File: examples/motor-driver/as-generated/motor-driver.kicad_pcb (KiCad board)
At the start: 2 copper layers, 88 x 50 mm, 19 parts, among them J1 VM 2.7-10.8V, J2 MOTOR A, J3 MOTOR B, J4 LOGIC, U1 DRV8833PW

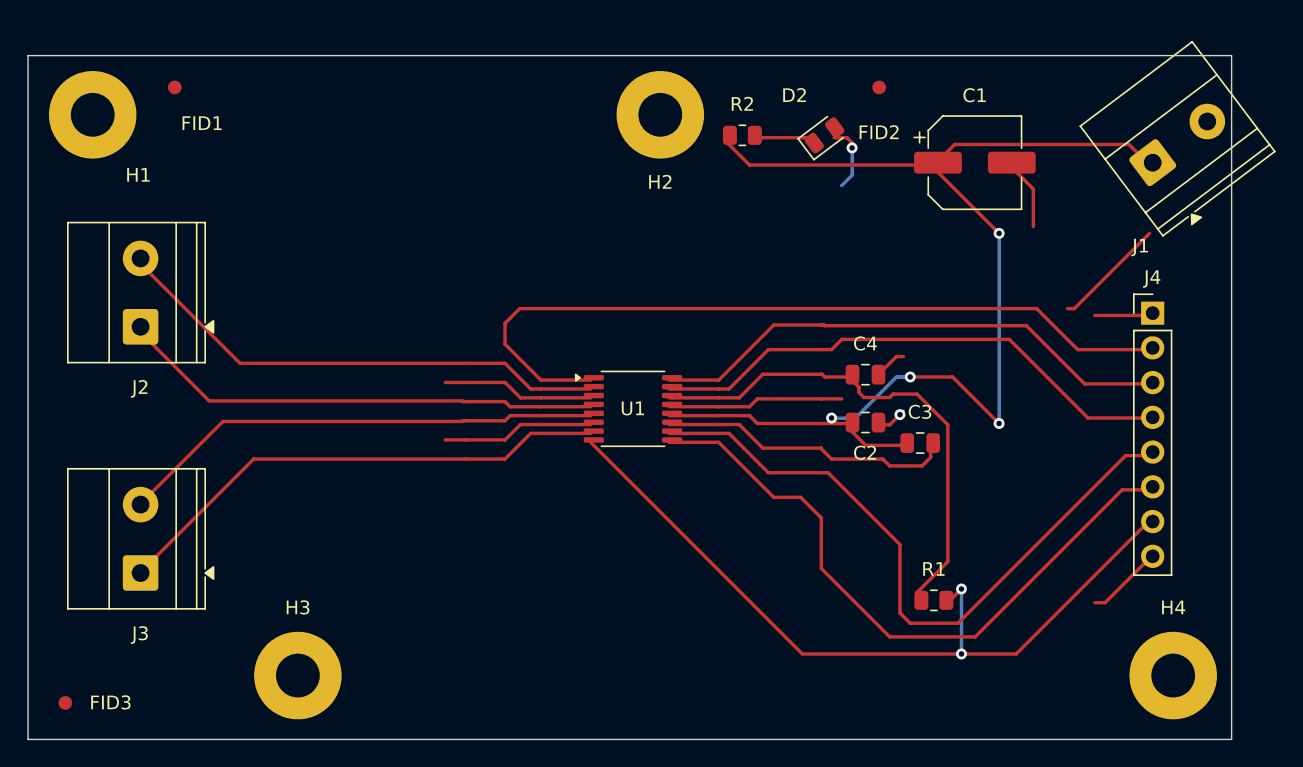
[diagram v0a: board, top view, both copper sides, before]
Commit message: Rebuild golden layouts and gate floorplan quality
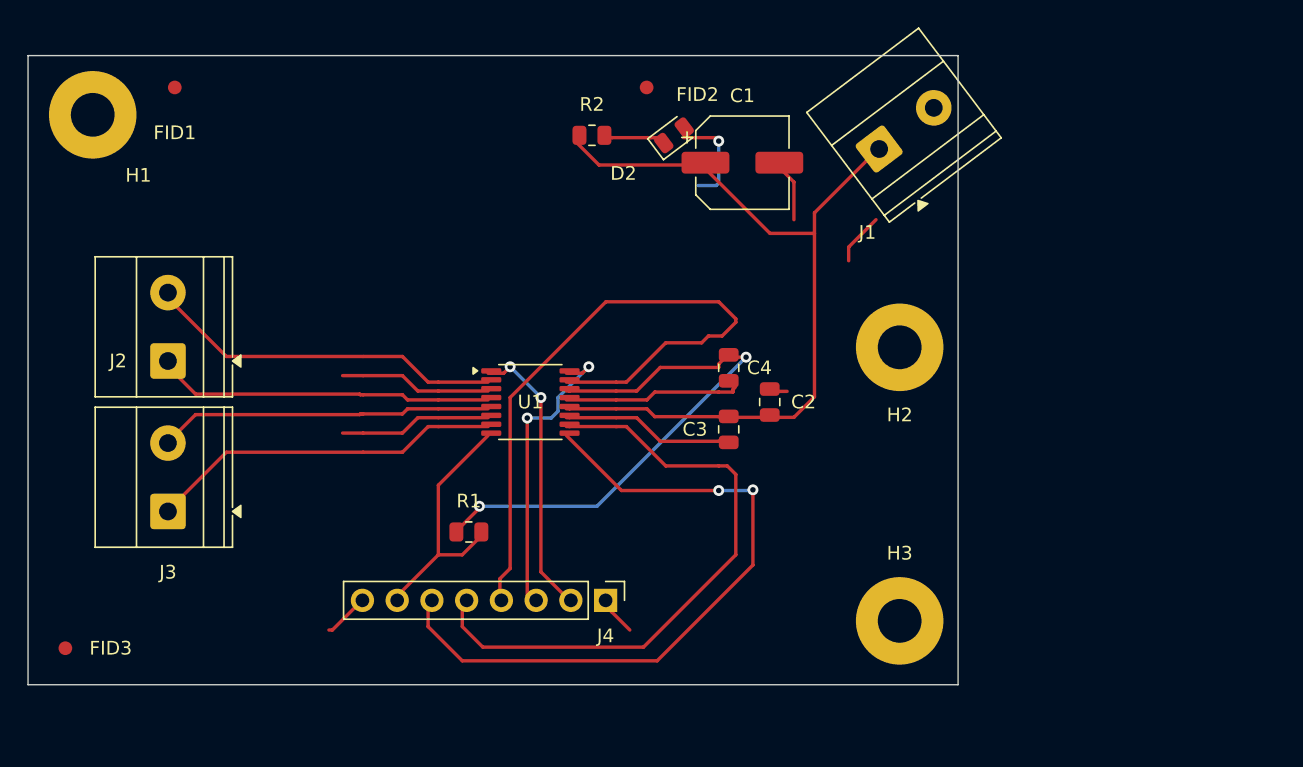
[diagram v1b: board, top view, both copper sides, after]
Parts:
- removed H4: M3, MountingHole:MountingHole_3.2mm_M3_Pad
- moved J4 45.2 mm to (142.2, 99.8), turned to 270 degrees
- moved H3 44.2 mm to (163.7, 101.3)
- moved R1 34.4 mm to (132.2, 94.8)
- moved H2 24.4 mm to (163.7, 81.3)
- moved J1 20.0 mm to (162.2, 66.8)
- moved C1 17.0 mm to (152.2, 67.8)
- moved FID2 17.0 mm to (145.2, 62.3), turned to 37 degrees
- moved C3 14.0 mm to (151.2, 87.3), turned to 270 degrees
- moved D2 11.0 mm to (147.2, 65.8)
- moved R2 11.0 mm to (141.2, 65.8)
- moved C4 10.0 mm to (151.2, 82.8), turned to 270 degrees
- moved U1 7.52 mm to (136.7, 85.3)
- moved C2 7.16 mm to (154.2, 85.3), turned to 90 degrees
- moved J3 4.92 mm to (110.2, 93.3)
- moved FID3 4.00 mm to (102.7, 103.3)
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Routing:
- net /nFAULT: track 57.7 -> 18.9 mm, vias 2 -> 0
- net /nSLEEP: track 57.7 -> 20.8 mm, vias 0 -> 2
- net /VM: track 87.9 -> 59.5 mm, vias 4 -> 0
- net /AIN1: track 38.6 -> 22.9 mm, vias 0 -> 2
- net /BOUT1: track 37.4 -> 26.3 mm
- net /BOUT2: track 35.9 -> 24.7 mm
- net /AOUT1: track 37.0 -> 26.3 mm
- net /AOUT2: track 35.5 -> 24.7 mm
- net /AIN2: track 39.1 -> 49.7 mm
- net /VCP: track 21.6 -> 12.5 mm
- net /LED_A: track 9.05 -> 4.15 mm, vias 1 -> 0
- net /VINT: track 37.1 -> 41.2 mm, vias 0 -> 2
- net GND: track 63.1 -> 59.1 mm
- net /BIN2: track 48.9 -> 44.9 mm
- net /BIN1: track 47.7 -> 50.3 mm, vias 0 -> 2
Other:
- board size 88 x 50 mm -> 68 x 46 mm

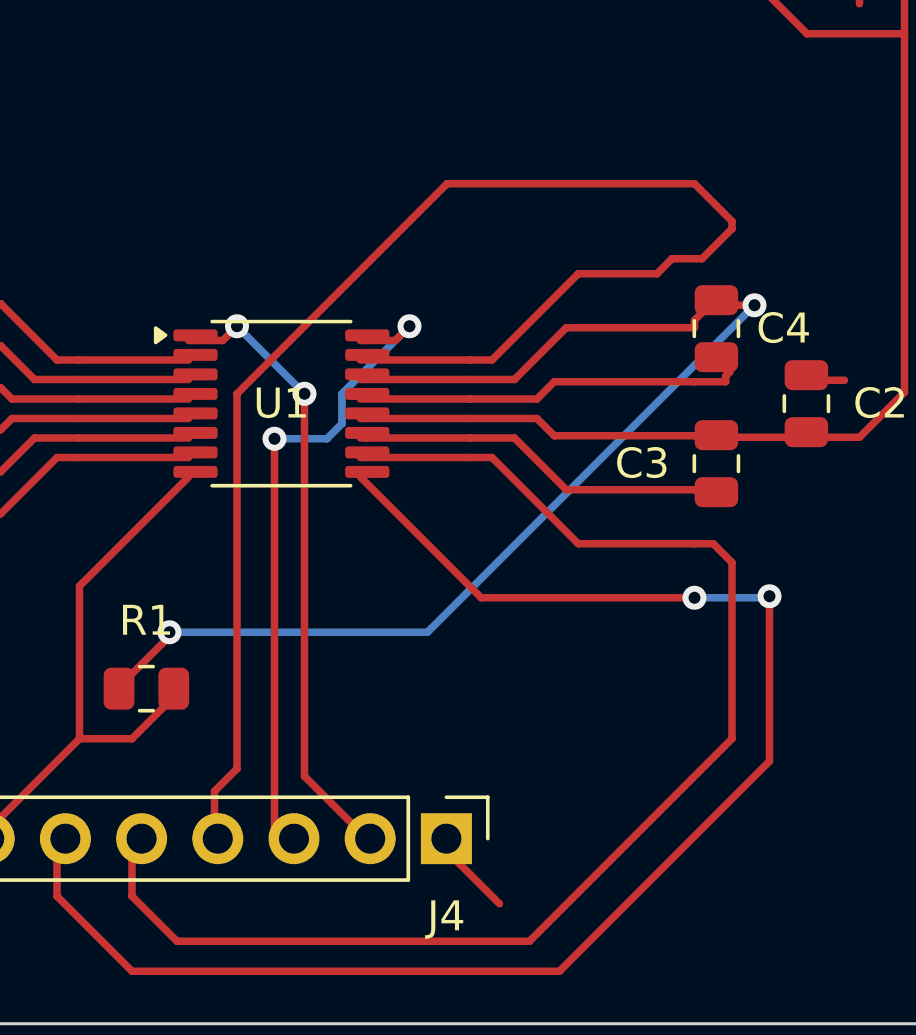
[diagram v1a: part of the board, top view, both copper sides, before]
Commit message: Use canonical fills and close motor return path
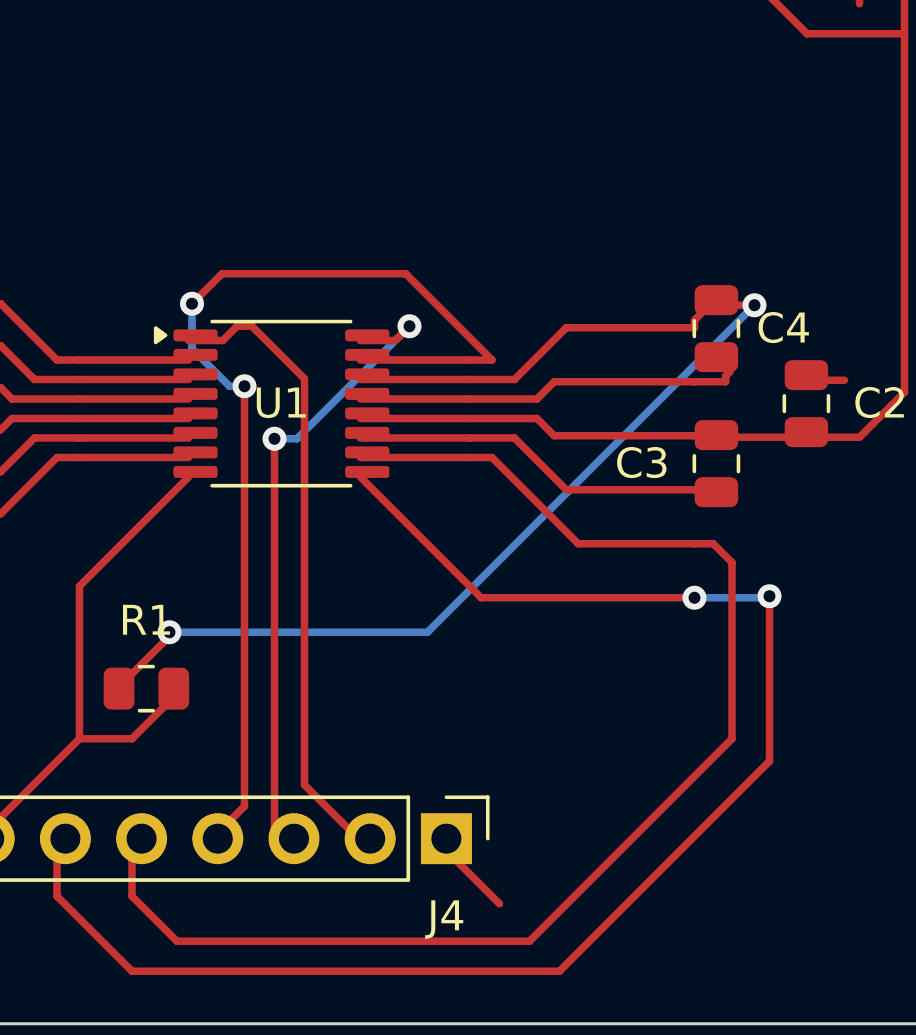
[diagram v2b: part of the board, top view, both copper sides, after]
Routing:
- net /AIN2: track 49.7 -> 35.5 mm, vias 0 -> 2
- net /AIN1: track 22.9 -> 21.6 mm
- net /nSLEEP: track 20.8 -> 21.1 mm, vias 2 -> 0
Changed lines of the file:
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@@
 	(segment (start 150.5 69.32) (end 150.32 69.5) (width 0.25) (layer "B.Cu") (net 1))
 	(segment (start 150.32 69.5) (end 149.0 69.5) (width 0.25) (layer "B.Cu") (net 1))
-	(segment (start 133.6375 83.225) (end 133.8675 83.225) (width 0.25) (layer "F.Cu") (net 15))
-	(segment (start 133.8675 83.225) (end 134.775 83.225) (width 0.25) (layer "F.Cu") (net 15))
-	(segment (start 134.775 83.225) (end 135.25 82.75) (width 0.25) (layer "F.Cu") (net 15))
 	(segment (start 133.6375 83.875) (end 130.0 83.875) (width 0.25) (layer "F.Cu") (net 4))
 	(segment (start 130.0 83.875) (end 129.25 83.875) (width 0.25) (layer "F.Cu") (net 4))
@@
 	(segment (start 133.6375 87.775) (end 130.0 91.4125) (width 0.25) (layer "F.Cu") (net 14))
 	(segment (start 130.0 91.4125) (end 130.0 96.5) (width 0.25) (layer "F.Cu") (net 14))
-	(segment (start 139.3625 83.225) (end 139.5925 83.225) (width 0.25) (layer "F.Cu") (net 2))
-	(segment (start 139.5925 83.225) (end 140.525 83.225) (width 0.25) (layer "F.Cu") (net 2))
-	(segment (start 140.525 83.225) (end 141.0 82.75) (width 0.25) (layer "F.Cu") (net 2))
 	(segment (start 139.3625 83.875) (end 139.5925 83.875) (width 0.25) (layer "F.Cu") (net 3))
 	(segment (start 139.5925 83.875) (end 143.0 83.875) (width 0.25) (layer "F.Cu") (net 3))
 	(segment (start 143.0 83.875) (end 143.75 83.875) (width 0.25) (layer "F.Cu") (net 3))
-	(segment (start 143.75 83.875) (end 146.625 81.0) (width 0.25) (layer "F.Cu") (net 3))
-	(segment (start 146.625 81.0) (end 149.25 81.0) (width 0.25) (layer "F.Cu") (net 3))
-	(segment (start 149.25 81.0) (end 149.75 80.5) (width 0.25) (layer "F.Cu") (net 3))
-	(segment (start 149.75 80.5) (end 150.75 80.5) (width 0.25) (layer "F.Cu") (net 3))
-	(segment (start 150.75 80.5) (end 151.75 79.5) (width 0.25) (layer "F.Cu") (net 3))
-	(segment (start 151.75 79.5) (end 151.75 79.25) (width 0.25) (layer "F.Cu") (net 3))
-	(segment (start 151.75 79.25) (end 150.5 78.0) (width 0.25) (layer "F.Cu") (net 3))
-	(segment (start 150.5 78.0) (end 142.25 78.0) (width 0.25) (layer "F.Cu") (net 3))
-	(segment (start 142.25 78.0) (end 135.25 85.0) (width 0.25) (layer "F.Cu") (net 3))
-	(segment (start 135.25 85.0) (end 135.25 97.5) (width 0.25) (layer "F.Cu") (net 3))
-	(segment (start 135.25 97.5) (end 134.5 98.25) (width 0.25) (layer "F.Cu") (net 3))
-	(segment (start 134.5 98.25) (end 134.5 99.75) (width 0.25) (layer "F.Cu") (net 3))
-	(segment (start 134.5 99.75) (end 134.5 99.83) (width 0.25) (layer "F.Cu") (net 3))
-	(segment (start 134.5 99.83) (end 134.5 99.88) (width 0.25) (layer "F.Cu") (net 3))
-	(segment (start 134.5 99.88) (end 134.38 100.0) (width 0.25) (layer "F.Cu") (net 3))
+	(segment (start 143.75 83.875) (end 140.875 81.0) (width 0.25) (layer "F.Cu") (net 3))
+	(segment (start 140.875 81.0) (end 134.75 81.0) (width 0.25) (layer "F.Cu") (net 3))
+	(segment (start 134.75 81.0) (end 133.75 82.0) (width 0.25) (layer "F.Cu") (net 3))
 	(segment (start 139.3625 84.525) (end 139.5925 84.525) (width 0.25) (layer "F.Cu") (net 12))
 	(segment (start 139.5925 84.525) (end 143.0 84.525) (width 0.25) (layer "F.Cu") (net 12))
@@
 	(segment (start 139.3625 87.775) (end 143.3875 91.8) (width 0.25) (layer "F.Cu") (net 6))
 	(segment (start 143.3875 91.8) (end 150.5 91.8) (width 0.25) (layer "F.Cu") (net 6))
+	(segment (start 139.3625 83.225) (end 139.5925 83.225) (width 0.25) (layer "F.Cu") (net 2))
+	(segment (start 139.5925 83.225) (end 140.525 83.225) (width 0.25) (layer "F.Cu") (net 2))
+	(segment (start 140.525 83.225) (end 141.0 82.75) (width 0.25) (layer "F.Cu") (net 2))
 	(segment (start 157.5 73.0) (end 157.5 71.5) (width 0.25) (layer "F.Cu") (net 13))
 	(segment (start 157.5 71.5) (end 161.2929 67.7071) (width 0.25) (layer "F.Cu") (net 13))
@@
 	(segment (start 145.5292 66.0) (end 145.7958 66.0) (width 0.25) (layer "F.Cu") (net 10))
 	(segment (start 145.7958 66.0) (end 146.0625 66.0) (width 0.25) (layer "F.Cu") (net 10))
-	(segment (start 141.0 82.75) (end 138.75 85.0) (width 0.25) (layer "B.Cu") (net 2))
-	(segment (start 138.75 85.0) (end 138.75 86.0) (width 0.25) (layer "B.Cu") (net 2))
-	(segment (start 138.75 86.0) (end 138.25 86.5) (width 0.25) (layer "B.Cu") (net 2))
-	(segment (start 138.25 86.5) (end 136.5 86.5) (width 0.25) (layer "B.Cu") (net 2))
-	(segment (start 136.5 86.5) (end 136.5 99.83) (width 0.25) (layer "F.Cu") (net 2))
-	(segment (start 136.5 99.83) (end 136.5 100.0) (width 0.25) (layer "F.Cu") (net 2))
-	(segment (start 136.5 100.0) (end 136.75 100.25) (width 0.25) (layer "F.Cu") (net 2))
-	(segment (start 136.75 100.25) (end 137.0 100.25) (width 0.25) (layer "F.Cu") (net 2))
-	(segment (start 137.0 100.25) (end 137.0 100.08) (width 0.25) (layer "F.Cu") (net 2))
-	(segment (start 137.0 100.08) (end 136.95 100.03) (width 0.25) (layer "F.Cu") (net 2))
-	(segment (start 136.95 100.03) (end 136.92 100.0) (width 0.25) (layer "F.Cu") (net 2))
+	(segment (start 141.0 82.75) (end 137.25 86.5) (width 0.25) (layer "B.Cu") (net 2))
+	(segment (start 137.25 86.5) (end 136.5 86.5) (width 0.25) (layer "B.Cu") (net 2))
+	(segment (start 136.5 86.5) (end 136.5 99.58) (width 0.25) (layer "F.Cu") (net 2))
+	(segment (start 136.5 99.58) (end 136.668 99.748) (width 0.25) (layer "F.Cu") (net 2))
+	(segment (start 136.668 99.748) (end 136.752 99.832) (width 0.25) (layer "F.Cu") (net 2))
+	(segment (start 136.752 99.832) (end 136.836 99.916) (width 0.25) (layer "F.Cu") (net 2))
+	(segment (start 136.836 99.916) (end 136.92 100.0) (width 0.25) (layer "F.Cu") (net 2))
+	(segment (start 133.75 82.0) (end 133.75 83.5) (width 0.25) (layer "B.Cu") (net 3))
+	(segment (start 133.75 83.5) (end 135.0 84.75) (width 0.25) (layer "B.Cu") (net 3))
+	(segment (start 135.0 84.75) (end 135.5 84.75) (width 0.25) (layer "B.Cu") (net 3))
+	(segment (start 135.5 84.75) (end 135.5 98.75) (width 0.25) (layer "F.Cu") (net 3))
+	(segment (start 135.5 98.75) (end 134.5 99.75) (width 0.25) (layer "F.Cu") (net 3))
+	(segment (start 134.5 99.75) (end 134.5 99.83) (width 0.25) (layer "F.Cu") (net 3))
+	(segment (start 134.5 99.83) (end 134.5 99.88) (width 0.25) (layer "F.Cu") (net 3))
+	(segment (start 134.5 99.88) (end 134.38 100.0) (width 0.25) (layer "F.Cu") (net 3))
 	(segment (start 150.5 91.8) (end 152.95 91.8) (width 0.25) (layer "B.Cu") (net 6))
 	(segment (start 152.95 91.8) (end 153.0 91.75) (width 0.25) (layer "B.Cu") (net 6))
@@
 	(segment (start 129.25 100.25) (end 129.25 100.05) (width 0.25) (layer "F.Cu") (net 6))
 	(segment (start 129.25 100.05) (end 129.3 100.0) (width 0.25) (layer "F.Cu") (net 6))
-	(segment (start 135.25 82.75) (end 137.5 85.0) (width 0.25) (layer "B.Cu") (net 15))
-	(segment (start 137.5 85.0) (end 137.5 97.75) (width 0.25) (layer "F.Cu") (net 15))
-	(segment (start 137.5 97.75) (end 139.5 99.75) (width 0.25) (layer "F.Cu") (net 15))
-	(segment (start 139.5 99.75) (end 139.5 99.83) (width 0.25) (layer "F.Cu") (net 15))
-	(segment (start 139.5 99.83) (end 139.5 99.96) (width 0.25) (layer "F.Cu") (net 15))
-	(segment (start 139.5 99.96) (end 139.46 100.0) (width 0.25) (layer "F.Cu") (net 15))
+	(segment (start 133.6375 83.225) (end 133.8675 83.225) (width 0.25) (layer "F.Cu") (net 15))
+	(segment (start 133.8675 83.225) (end 134.775 83.225) (width 0.25) (layer "F.Cu") (net 15))
+	(segment (start 134.775 83.225) (end 135.25 82.75) (width 0.25) (layer "F.Cu") (net 15))
+	(segment (start 135.25 82.75) (end 135.75 82.75) (width 0.25) (layer "F.Cu") (net 15))
+	(segment (start 135.75 82.75) (end 137.5 84.5) (width 0.25) (layer "F.Cu") (net 15))
+	(segment (start 137.5 84.5) (end 137.5 98.04) (width 0.25) (layer "F.Cu") (net 15))
+	(segment (start 137.5 98.04) (end 138.7529 99.2929) (width 0.25) (layer "F.Cu") (net 15))
+	(segment (start 138.7529 99.2929) (end 138.9886 99.5286) (width 0.25) (layer "F.Cu") (net 15))
+	(segment (start 138.9886 99.5286) (end 139.2243 99.7643) (width 0.25) (layer "F.Cu") (net 15))
+	(segment (start 139.2243 99.7643) (end 139.46 100.0) (width 0.25) (layer "F.Cu") (net 15))
 	(segment (start 132.9125 95.0) (end 132.9125 95.1625) (width 0.25) (layer "F.Cu") (net 14))
 	(segment (start 132.9125 95.1625) (end 133.0 95.25) (width 0.25) (layer "F.Cu") (net 14))
@@
 	(via (at 136.5 86.5) (size 0.8) (drill 0.4) (layers "F.Cu" "B.Cu") (net 2))
 	(via (at 141.0 82.75) (size 0.8) (drill 0.4) (layers "F.Cu" "B.Cu") (net 2))
+	(via (at 133.75 82.0) (size 0.8) (drill 0.4) (layers "F.Cu" "B.Cu") (net 3))
+	(via (at 135.5 84.75) (size 0.8) (drill 0.4) (layers "F.Cu" "B.Cu") (net 3))
 	(via (at 150.5 91.8) (size 0.8) (drill 0.4) (layers "F.Cu" "B.Cu") (net 6))
 	(via (at 153.0 91.75) (size 0.8) (drill 0.4) (layers "F.Cu" "B.Cu") (net 6))
@@
 	(via (at 133.0 92.95) (size 0.8) (drill 0.4) (layers "F.Cu" "B.Cu") (net 12))
 	(via (at 152.5 82.05) (size 0.8) (drill 0.4) (layers "F.Cu" "B.Cu") (net 12))
-	(via (at 135.25 82.75) (size 0.8) (drill 0.4) (layers "F.Cu" "B.Cu") (net 15))
-	(via (at 137.5 85.0) (size 0.8) (drill 0.4) (layers "F.Cu" "B.Cu") (net 15))
 )

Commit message: Finalize deterministic golden regeneration
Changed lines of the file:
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@@
 	(segment (start 133.6375 87.775) (end 130.0 91.4125) (width 0.25) (layer "F.Cu") (net 14))
 	(segment (start 130.0 91.4125) (end 130.0 96.5) (width 0.25) (layer "F.Cu") (net 14))
-	(segment (start 139.3625 83.875) (end 139.5925 83.875) (width 0.25) (layer "F.Cu") (net 3))
-	(segment (start 139.5925 83.875) (end 143.0 83.875) (width 0.25) (layer "F.Cu") (net 3))
-	(segment (start 143.0 83.875) (end 143.75 83.875) (width 0.25) (layer "F.Cu") (net 3))
-	(segment (start 143.75 83.875) (end 140.875 81.0) (width 0.25) (layer "F.Cu") (net 3))
-	(segment (start 140.875 81.0) (end 134.75 81.0) (width 0.25) (layer "F.Cu") (net 3))
-	(segment (start 134.75 81.0) (end 133.75 82.0) (width 0.25) (layer "F.Cu") (net 3))
 	(segment (start 139.3625 84.525) (end 139.5925 84.525) (width 0.25) (layer "F.Cu") (net 12))
 	(segment (start 139.5925 84.525) (end 143.0 84.525) (width 0.25) (layer "F.Cu") (net 12))
@@
 	(segment (start 139.5925 83.225) (end 140.525 83.225) (width 0.25) (layer "F.Cu") (net 2))
 	(segment (start 140.525 83.225) (end 141.0 82.75) (width 0.25) (layer "F.Cu") (net 2))
+	(segment (start 139.3625 83.875) (end 139.5925 83.875) (width 0.25) (layer "F.Cu") (net 3))
+	(segment (start 139.5925 83.875) (end 143.75 83.875) (width 0.25) (layer "F.Cu") (net 3))
+	(segment (start 143.75 83.875) (end 146.625 81.0) (width 0.25) (layer "F.Cu") (net 3))
 	(segment (start 157.5 73.0) (end 157.5 71.5) (width 0.25) (layer "F.Cu") (net 13))
 	(segment (start 157.5 71.5) (end 161.2929 67.7071) (width 0.25) (layer "F.Cu") (net 13))
@@
 	(segment (start 136.752 99.832) (end 136.836 99.916) (width 0.25) (layer "F.Cu") (net 2))
 	(segment (start 136.836 99.916) (end 136.92 100.0) (width 0.25) (layer "F.Cu") (net 2))
-	(segment (start 133.75 82.0) (end 133.75 83.5) (width 0.25) (layer "B.Cu") (net 3))
-	(segment (start 133.75 83.5) (end 135.0 84.75) (width 0.25) (layer "B.Cu") (net 3))
-	(segment (start 135.0 84.75) (end 135.5 84.75) (width 0.25) (layer "B.Cu") (net 3))
-	(segment (start 135.5 84.75) (end 135.5 98.75) (width 0.25) (layer "F.Cu") (net 3))
-	(segment (start 135.5 98.75) (end 134.5 99.75) (width 0.25) (layer "F.Cu") (net 3))
-	(segment (start 134.5 99.75) (end 134.5 99.83) (width 0.25) (layer "F.Cu") (net 3))
-	(segment (start 134.5 99.83) (end 134.5 99.88) (width 0.25) (layer "F.Cu") (net 3))
-	(segment (start 134.5 99.88) (end 134.38 100.0) (width 0.25) (layer "F.Cu") (net 3))
+	(segment (start 146.625 81.0) (end 140.375 87.25) (width 0.25) (layer "B.Cu") (net 3))
+	(segment (start 140.375 87.25) (end 135.5 87.25) (width 0.25) (layer "B.Cu") (net 3))
+	(segment (start 135.5 87.25) (end 135.5 98.88) (width 0.25) (layer "F.Cu") (net 3))
+	(segment (start 135.5 98.88) (end 135.052 99.328) (width 0.25) (layer "F.Cu") (net 3))
+	(segment (start 135.052 99.328) (end 134.828 99.552) (width 0.25) (layer "F.Cu") (net 3))
+	(segment (start 134.828 99.552) (end 134.604 99.776) (width 0.25) (layer "F.Cu") (net 3))
+	(segment (start 134.604 99.776) (end 134.58 99.8) (width 0.25) (layer "F.Cu") (net 3))
+	(segment (start 134.58 99.8) (end 134.38 100.0) (width 0.25) (layer "F.Cu") (net 3))
 	(segment (start 150.5 91.8) (end 152.95 91.8) (width 0.25) (layer "B.Cu") (net 6))
 	(segment (start 152.95 91.8) (end 153.0 91.75) (width 0.25) (layer "B.Cu") (net 6))
@@
 	(via (at 136.5 86.5) (size 0.8) (drill 0.4) (layers "F.Cu" "B.Cu") (net 2))
 	(via (at 141.0 82.75) (size 0.8) (drill 0.4) (layers "F.Cu" "B.Cu") (net 2))
-	(via (at 133.75 82.0) (size 0.8) (drill 0.4) (layers "F.Cu" "B.Cu") (net 3))
-	(via (at 135.5 84.75) (size 0.8) (drill 0.4) (layers "F.Cu" "B.Cu") (net 3))
+	(via (at 135.5 87.25) (size 0.8) (drill 0.4) (layers "F.Cu" "B.Cu") (net 3))
+	(via (at 146.625 81.0) (size 0.8) (drill 0.4) (layers "F.Cu" "B.Cu") (net 3))
 	(via (at 150.5 91.8) (size 0.8) (drill 0.4) (layers "F.Cu" "B.Cu") (net 6))
 	(via (at 153.0 91.75) (size 0.8) (drill 0.4) (layers "F.Cu" "B.Cu") (net 6))

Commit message: Close manufacturing and escape-route findings
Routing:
- net /LED_A: track 4.15 -> 11.6 mm, vias 0 -> 1
- net GND: track 59.1 -> 51.6 mm, vias 1 -> 0
